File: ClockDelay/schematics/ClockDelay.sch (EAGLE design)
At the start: 72 parts, among them IC1 TL072P, IC2 MEGA168, Q301 2N3904, Q401 2N3904, Q501 2N3904, Q601 2N3904, Q701 2N3904, Y1 16Mhz

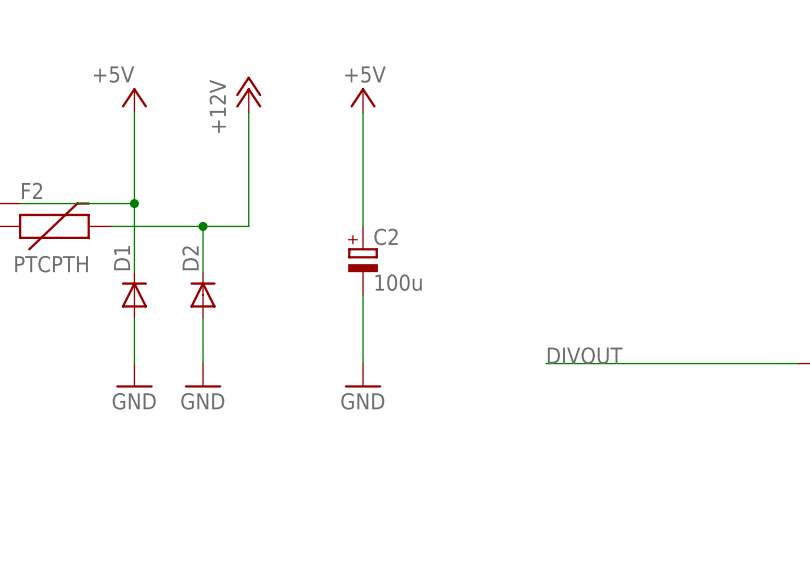
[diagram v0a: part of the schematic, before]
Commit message: changed to 10uF decoupling capacitor
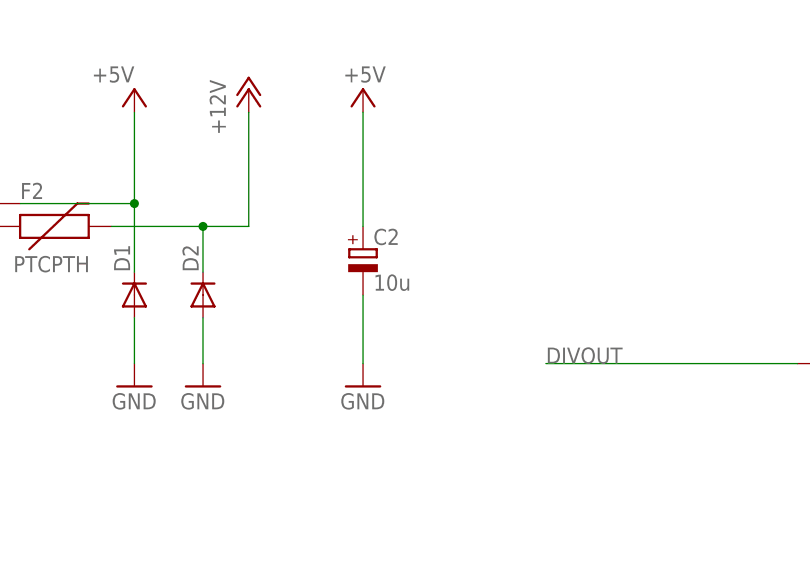
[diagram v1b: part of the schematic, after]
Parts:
- C2: value 100u -> 10u
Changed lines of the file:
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@@
 <part name="D1" library="Rebel" deviceset="DIODE" device="1N4001"/>
 <part name="U$2" library="SparkFun" deviceset="M08X2" device=""/>
-<part name="C2" library="rcl" deviceset="CPOL-EU" device="E5-6" value="100u"/>
+<part name="C2" library="rcl" deviceset="CPOL-EU" device="E5-6" value="10u"/>
 <part name="D2" library="Rebel" deviceset="DIODE" device="1N4001"/>
 <part name="F1" library="Rebel" deviceset="PTC" device="PTH"/>

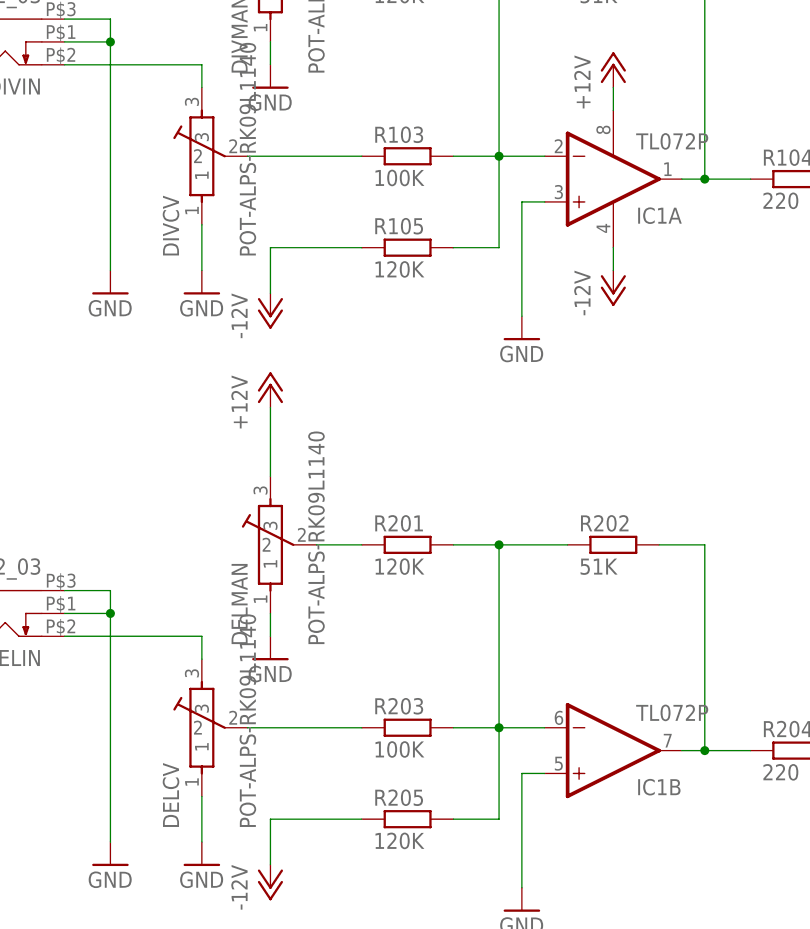
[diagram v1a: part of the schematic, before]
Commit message: changed R103 and R203 from 100K to 51K
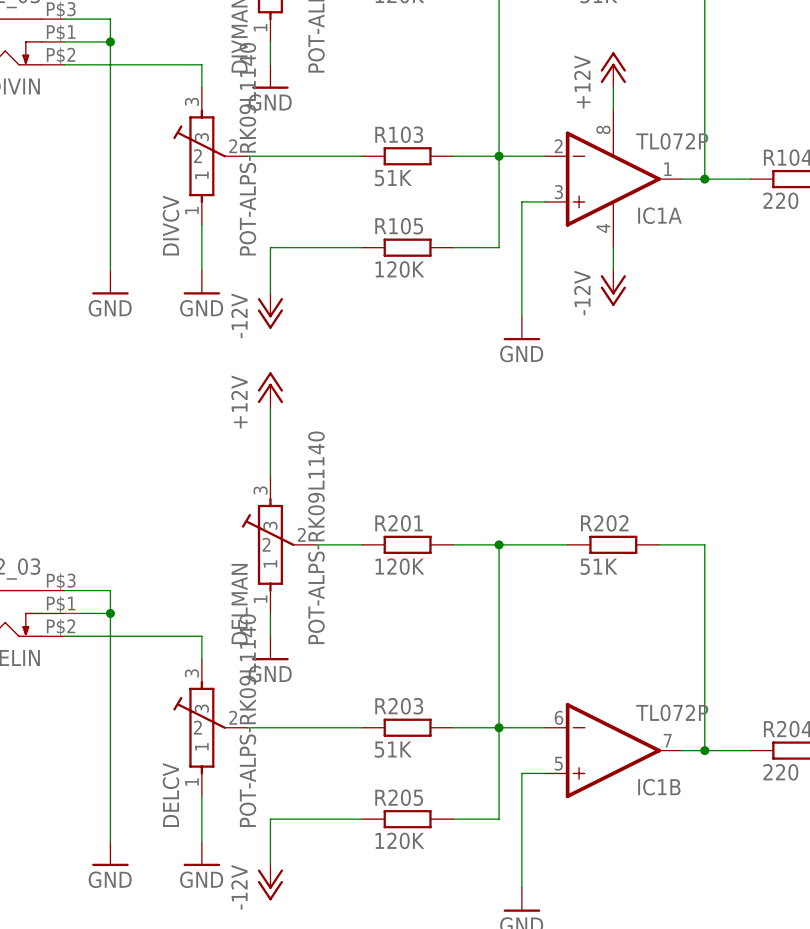
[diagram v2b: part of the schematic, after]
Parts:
- R103, R203: value 100K -> 51K
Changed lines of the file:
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@@
 <part name="R102" library="Rebel" deviceset="R-EU_" device="0204/7" value="51K"/>
 <part name="R101" library="Rebel" deviceset="R-EU_" device="0204/7" value="120K"/>
-<part name="R103" library="Rebel" deviceset="R-EU_" device="0204/7" value="100K"/>
+<part name="R103" library="Rebel" deviceset="R-EU_" device="0204/7" value="51K"/>
 <part name="R104" library="Rebel" deviceset="R-EU_" device="0204/7" value="220"/>
 <part name="DIVIN" library="Rebel" deviceset="CON-LUMBERG_1502_03" device=""/>
@@
 <part name="R202" library="Rebel" deviceset="R-EU_" device="0204/7" value="51K"/>
 <part name="R201" library="Rebel" deviceset="R-EU_" device="0204/7" value="120K"/>
-<part name="R203" library="Rebel" deviceset="R-EU_" device="0204/7" value="100K"/>
+<part name="R203" library="Rebel" deviceset="R-EU_" device="0204/7" value="51K"/>
 <part name="R204" library="Rebel" deviceset="R-EU_" device="0204/7" value="220"/>
 <part name="DELIN" library="Rebel" deviceset="CON-LUMBERG_1502_03" device=""/>

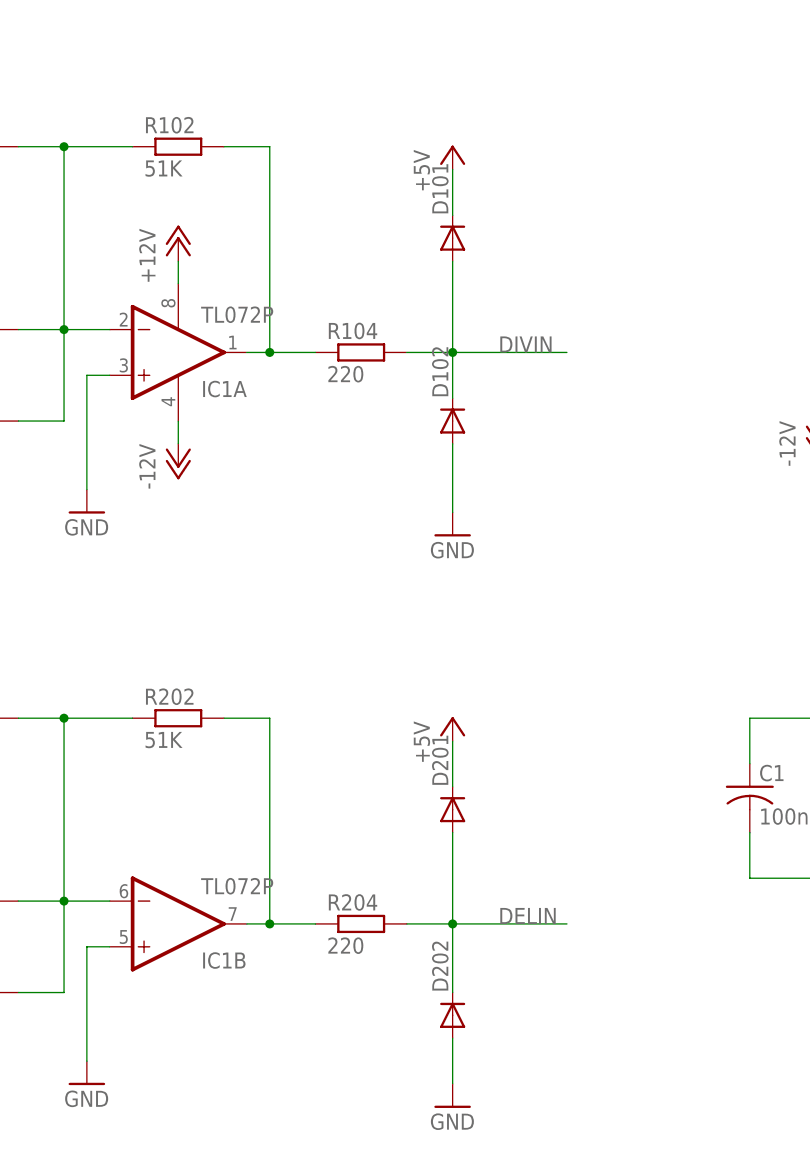
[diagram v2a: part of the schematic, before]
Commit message: changed ADC input resistor values and DNC'd diodes
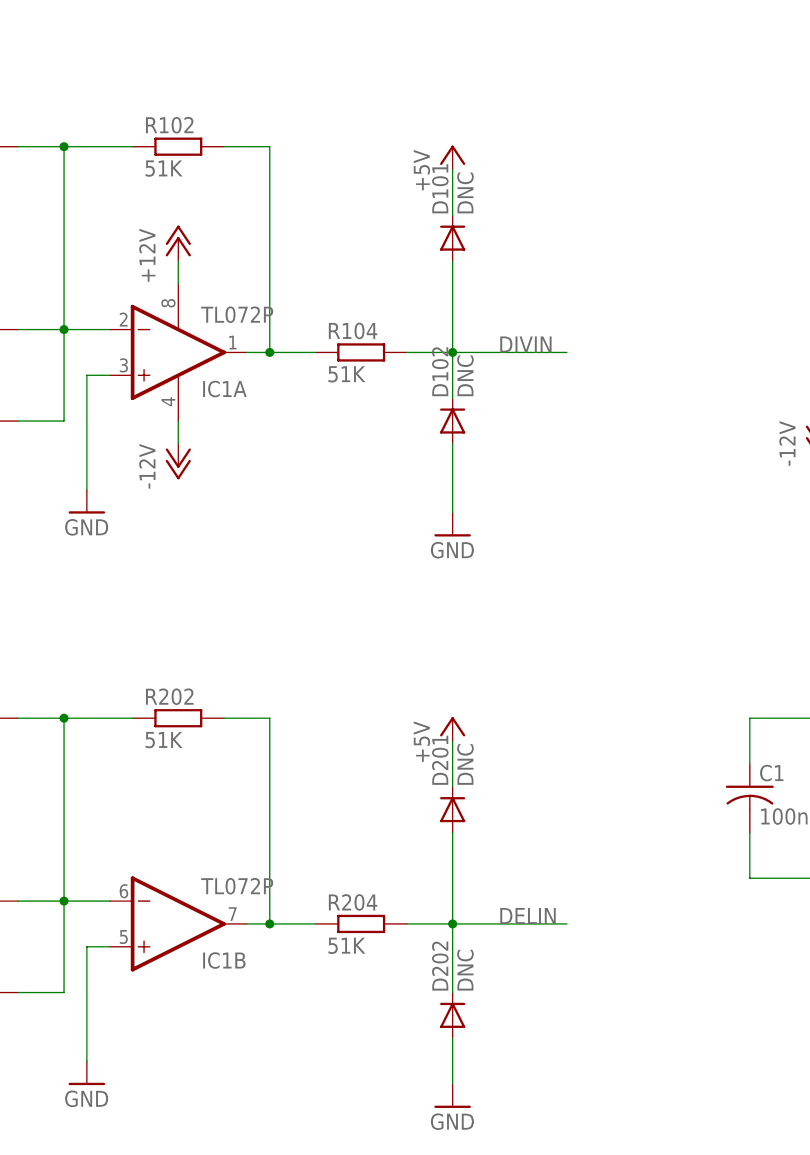
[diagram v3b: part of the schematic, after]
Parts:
- D101, D102, D201, D202: value (none) -> DNC
- R104, R204: value 220 -> 51K
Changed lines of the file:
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@@
 <part name="R101" library="Rebel" deviceset="R-EU_" device="0204/7" value="120K"/>
 <part name="R103" library="Rebel" deviceset="R-EU_" device="0204/7" value="51K"/>
-<part name="R104" library="Rebel" deviceset="R-EU_" device="0204/7" value="220"/>
+<part name="R104" library="Rebel" deviceset="R-EU_" device="0204/7" value="51K"/>
 <part name="DIVIN" library="Rebel" deviceset="CON-LUMBERG_1502_03" device=""/>
 <part name="GND2" library="supply1" deviceset="GND" device=""/>
@@
 <part name="GND1" library="supply1" deviceset="GND" device=""/>
 <part name="GND4" library="supply1" deviceset="GND" device=""/>
-<part name="D101" library="Rebel" deviceset="DIODE" device="1N4148"/>
+<part name="D101" library="Rebel" deviceset="DIODE" device="1N4148" value="DNC"/>
 <part name="P+1" library="supply1" deviceset="+12V" device=""/>
 <part name="P+3" library="supply1" deviceset="+5V" device=""/>
@@
 <part name="R201" library="Rebel" deviceset="R-EU_" device="0204/7" value="120K"/>
 <part name="R203" library="Rebel" deviceset="R-EU_" device="0204/7" value="51K"/>
-<part name="R204" library="Rebel" deviceset="R-EU_" device="0204/7" value="220"/>
+<part name="R204" library="Rebel" deviceset="R-EU_" device="0204/7" value="51K"/>
 <part name="DELIN" library="Rebel" deviceset="CON-LUMBERG_1502_03" device=""/>
 <part name="GND5" library="supply1" deviceset="GND" device=""/>
@@
 <part name="GND7" library="supply1" deviceset="GND" device=""/>
 <part name="GND8" library="supply1" deviceset="GND" device=""/>
-<part name="D201" library="Rebel" deviceset="DIODE" device="1N4148"/>
+<part name="D201" library="Rebel" deviceset="DIODE" device="1N4148" value="DNC"/>
 <part name="P+5" library="supply1" deviceset="+12V" device=""/>
 <part name="P+6" library="supply1" deviceset="+5V" device=""/>
@@
 <part name="P+11" library="supply1" deviceset="+12V" device=""/>
 <part name="GND29" library="supply1" deviceset="GND" device=""/>
-<part name="D102" library="Rebel" deviceset="DIODE" device="1N4148"/>
-<part name="D202" library="Rebel" deviceset="DIODE" device="1N4148"/>
+<part name="D102" library="Rebel" deviceset="DIODE" device="1N4148" value="DNC"/>
+<part name="D202" library="Rebel" deviceset="DIODE" device="1N4148" value="DNC"/>
 <part name="GND30" library="supply1" deviceset="GND" device=""/>
 <part name="GND31" library="supply1" deviceset="GND" device=""/>
